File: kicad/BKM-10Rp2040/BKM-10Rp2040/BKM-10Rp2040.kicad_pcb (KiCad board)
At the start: 2 copper layers, 34.3 x 82.5 mm, 12 parts, among them J1 DB9_Female_MountingHoles, J2 Conn_01x04, SW1 SW_DPST_x2, U1 ADM3063EARZ-ND, U2 Pico, U3 TSOP335xx

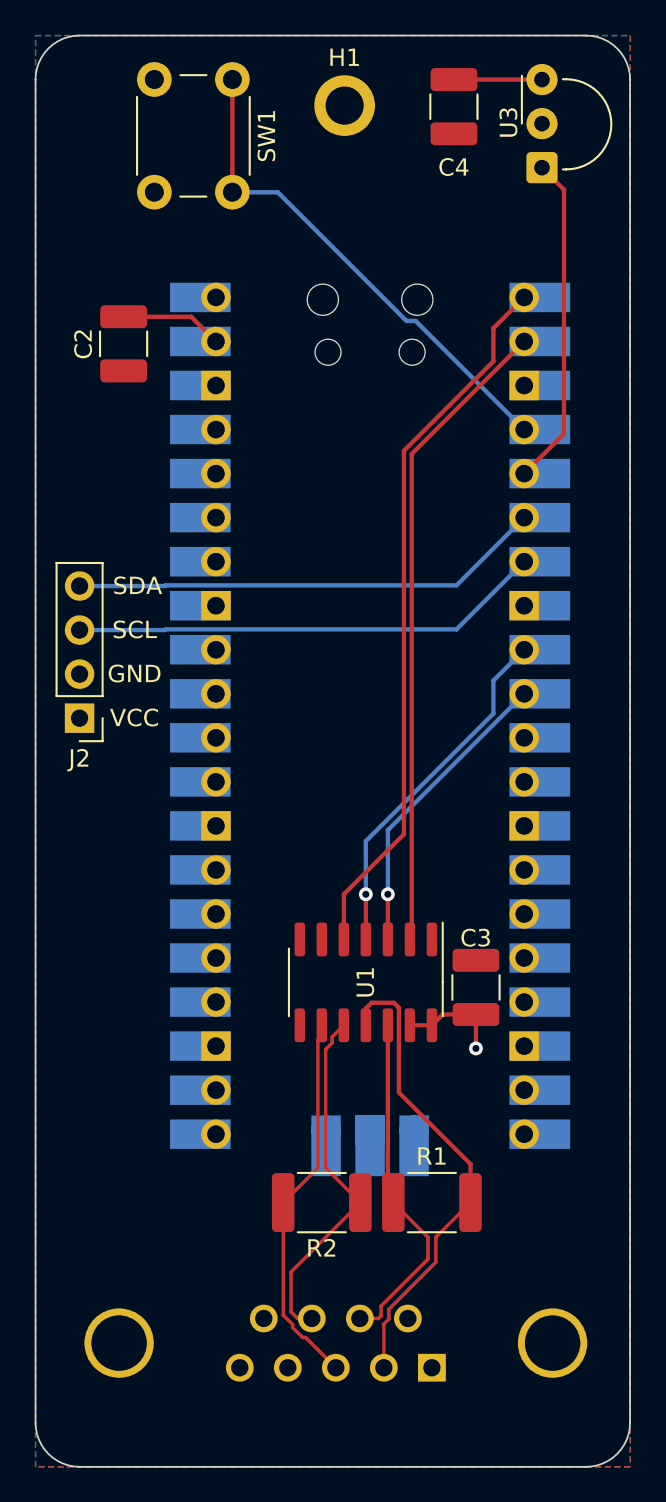
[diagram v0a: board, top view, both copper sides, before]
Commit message: add 2 layer PBC and also a RP2040 version
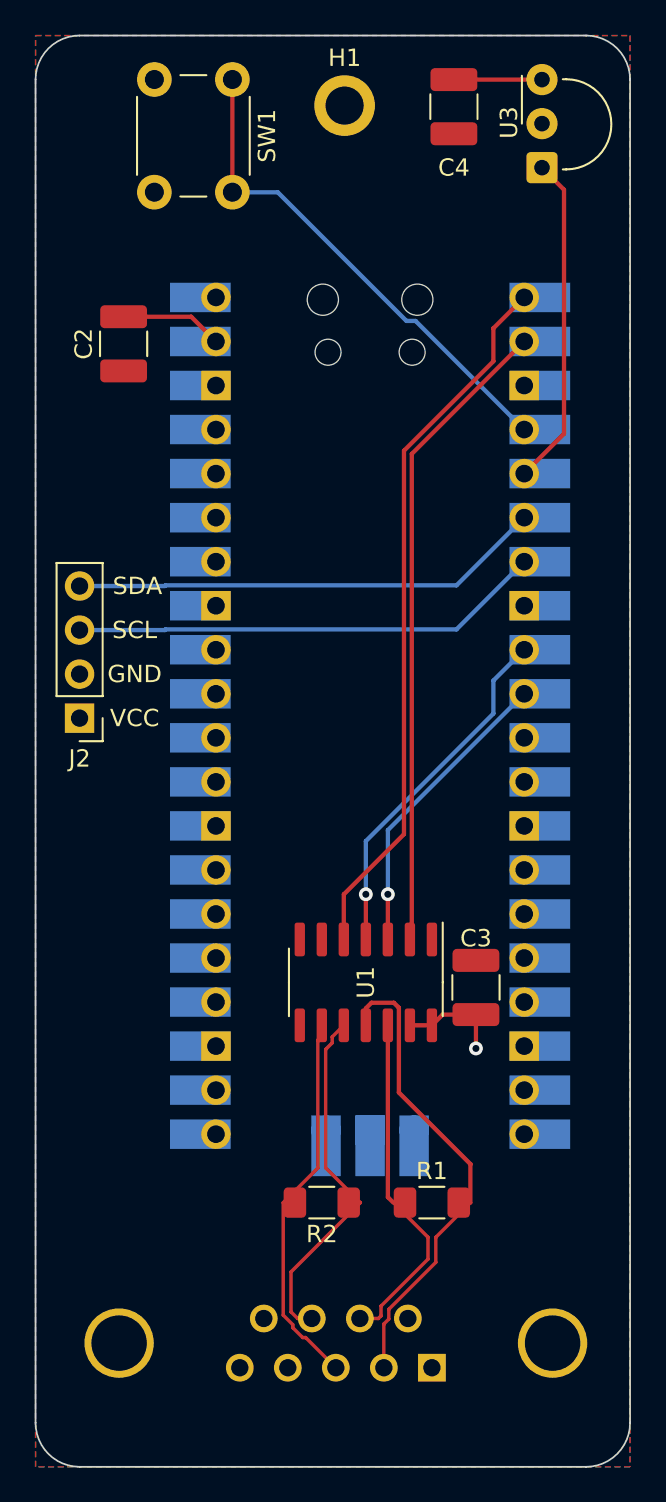
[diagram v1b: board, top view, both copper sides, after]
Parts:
- R1, R2: footprint Resistor_SMD:R_1812_4532Metric_Pad1.30x3.40mm_HandSolder -> Resistor_SMD:R_1206_3216Metric_Pad1.30x1.75mm_HandSolder
